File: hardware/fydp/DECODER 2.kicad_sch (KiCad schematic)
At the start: 29 parts, among them J2 Conn_01x02_Pin, J6 Conn_01x04_Pin, U55 74HC154D

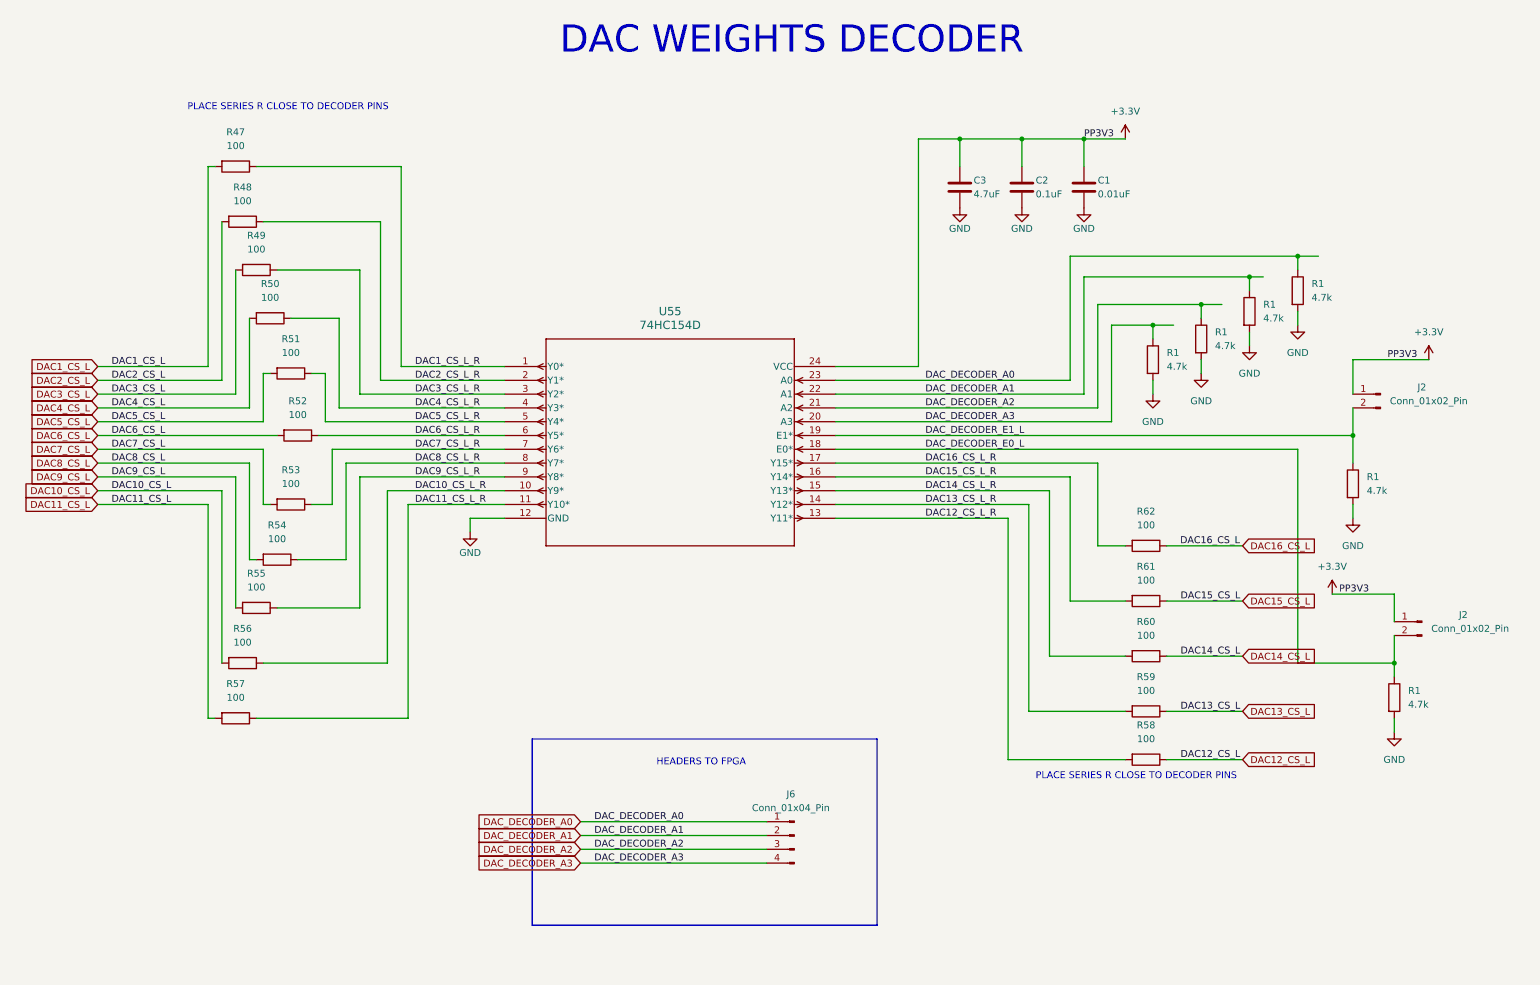
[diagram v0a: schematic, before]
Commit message: Remove 2 channels of multiplier and change ADC
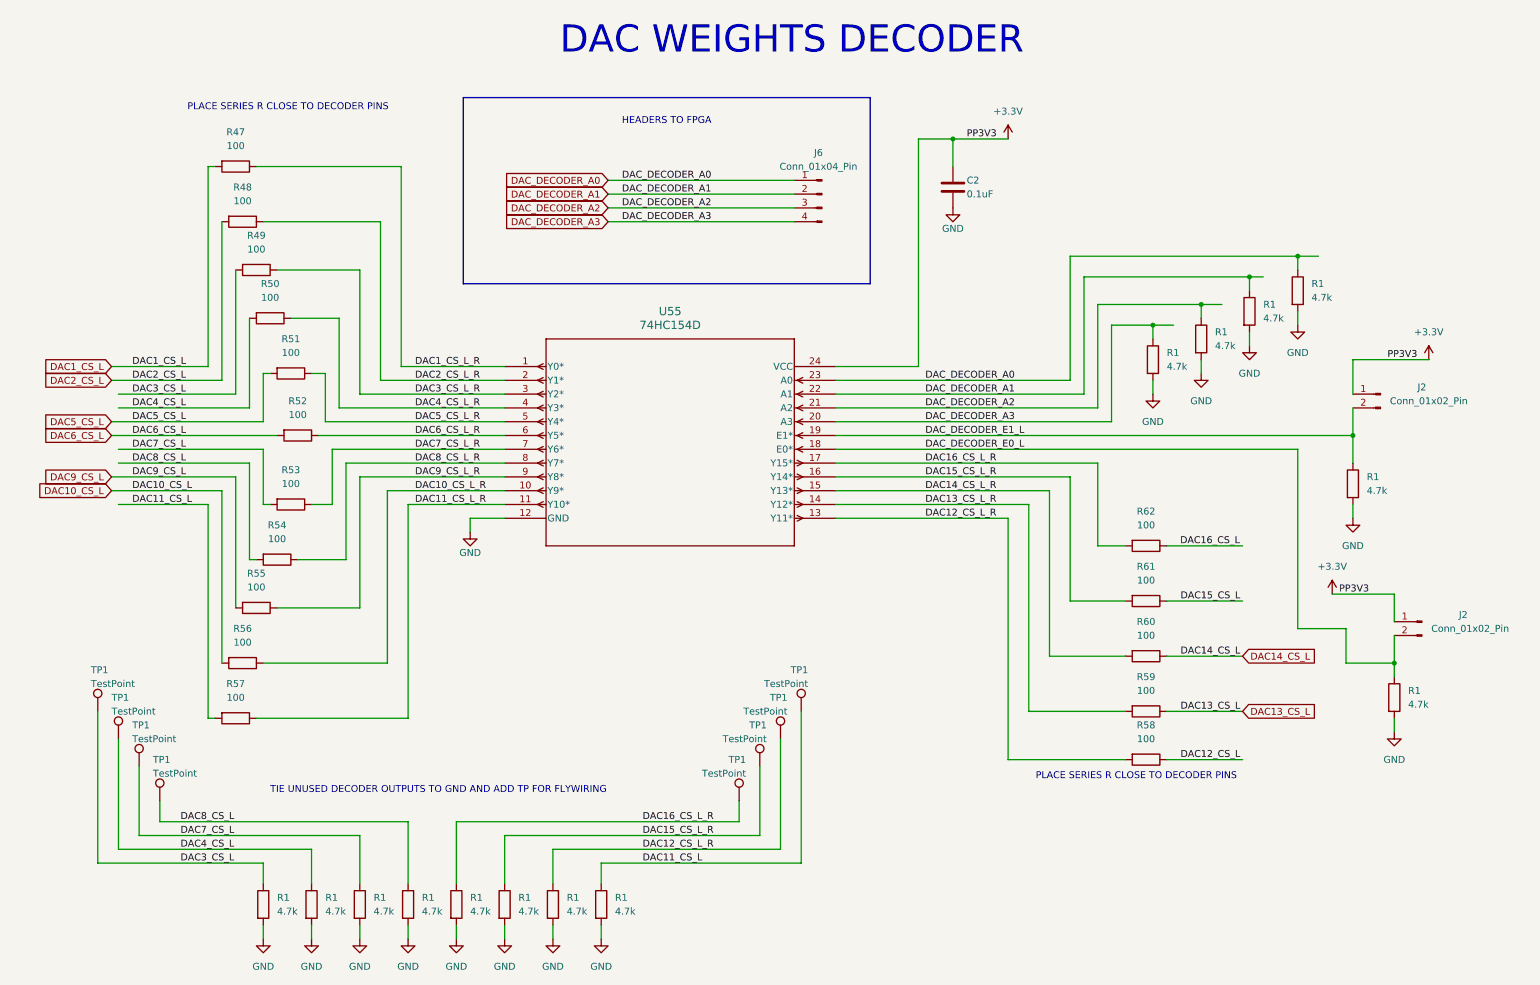
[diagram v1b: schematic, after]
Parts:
- removed C1: 0.01uF, Capacitor_SMD:C_0805_2012Metric, symbol Device:C
- removed C3: 4.7uF, Capacitor_SMD:C_0805_2012Metric, symbol Device:C
- added R1 (x8): 4.7k, Resistor_SMD:R_0805_2012Metric, symbol Device:R
- added TP1 (x8): TestPoint, TestPoint:TestPoint_Pad_1.0x1.0mm, symbol Connector:TestPoint
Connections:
- net DAC11_CS_L: now also R1.1, TP1.1
- net DAC12_CS_L_R: now also R1.1, TP1.1
- net DAC15_CS_L_R: now also R1.1, TP1.1
- net DAC16_CS_L_R: now also R1.1, TP1.1
- net DAC3_CS_L: now also R1.1, TP1.1
- net DAC4_CS_L: now also R1.1, TP1.1
- net DAC7_CS_L: now also R1.1, TP1.1
- net DAC8_CS_L: now also R1.1, TP1.1
- net GND: now also R1.2, R1.2, R1.2, R1.2, R1.2, R1.2, R1.2, R1.2
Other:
- note added: "TIE UNUSED DECODER OUTPUTS TO GND AND ADD TP FOR FLYWIRING"
- moved on the sheet: C2, J6

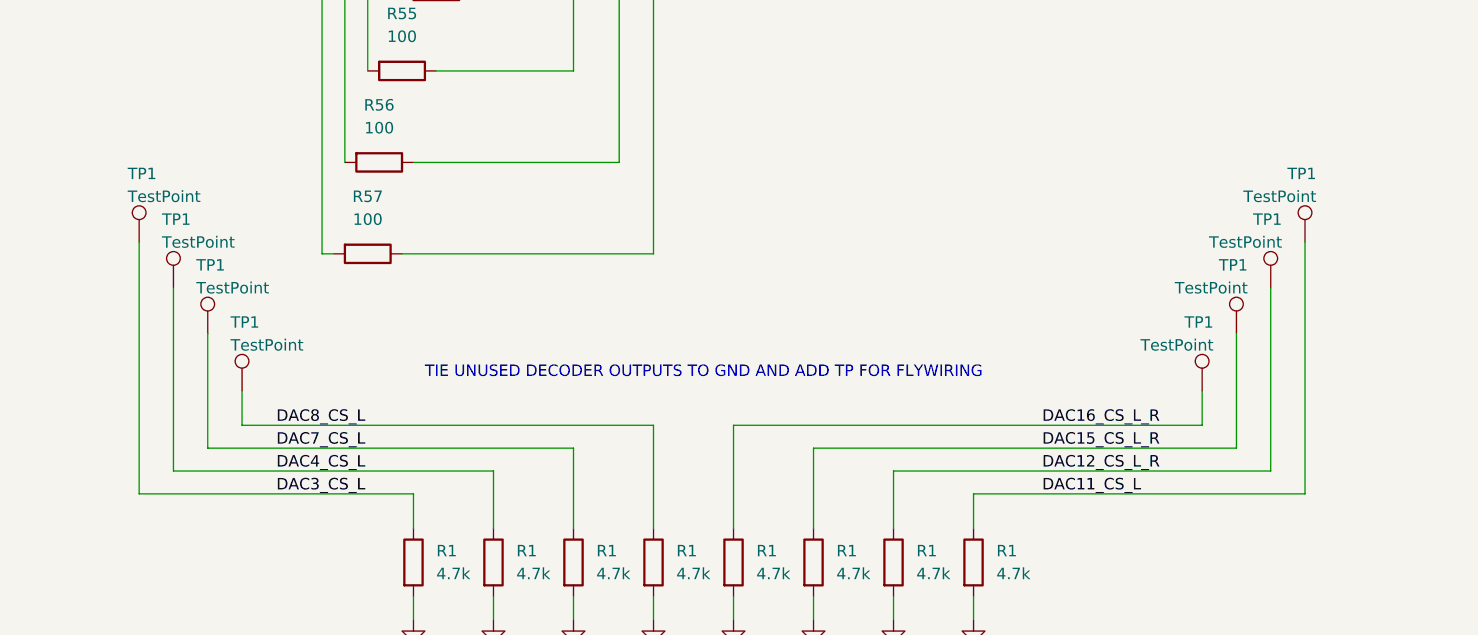
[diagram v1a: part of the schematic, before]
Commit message: Initial layout mostly complete, need to complete lots of routing
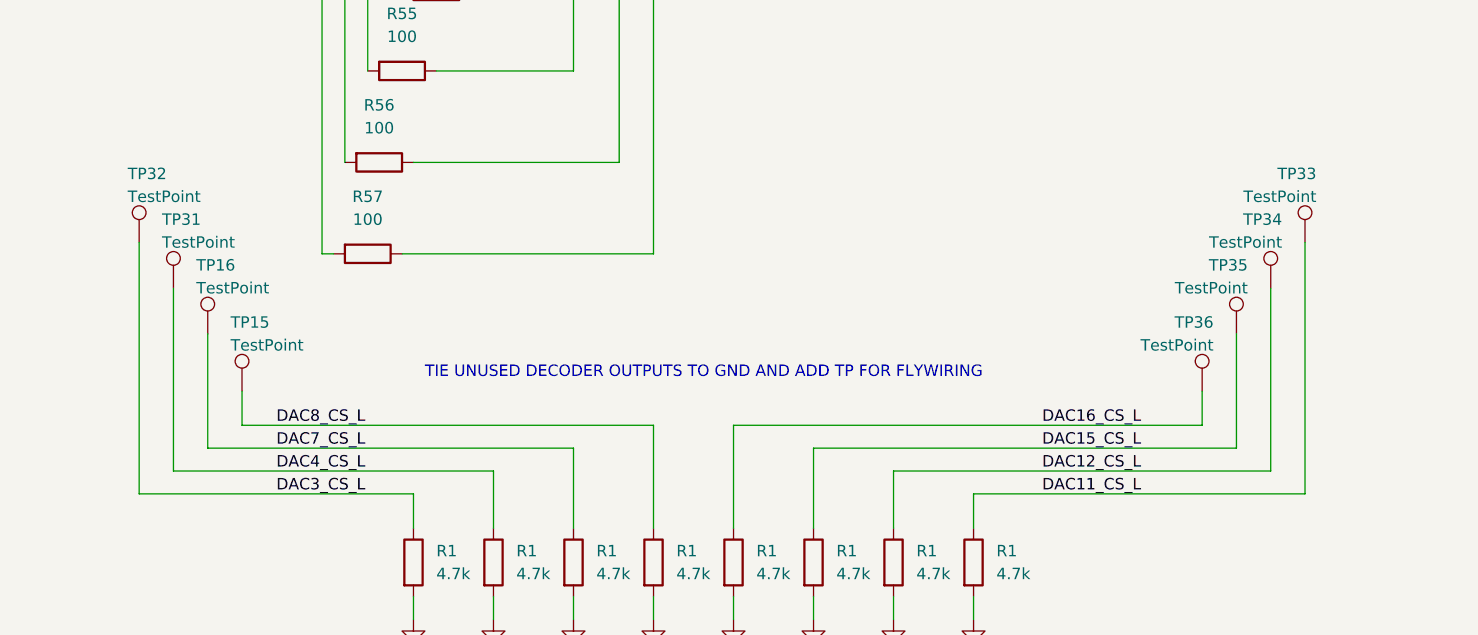
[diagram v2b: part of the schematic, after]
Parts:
- renumbered TP1 to TP15, TP1 to TP16, TP1 to TP31, TP1 to TP32, TP1 to TP33, TP1 to TP34, TP1 to TP35, TP1 to TP36
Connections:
- net DAC12_CS_L: now also R1.1, TP34.1
- net DAC12_CS_L_R: no longer R1.1, TP34.1
- net DAC15_CS_L: now also R1.1, TP35.1
- net DAC15_CS_L_R: no longer R1.1, TP35.1
- net DAC16_CS_L: now also R1.1, TP36.1
- net DAC16_CS_L_R: no longer R1.1, TP36.1
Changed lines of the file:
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@@
     (effects (font (size 1.27 1.27)) (justify left bottom))
   )
-  (label "DAC12_CS_L_R" (at 123.19 171.45 0) (fields_autoplaced)
+  (label "DAC12_CS_L" (at 123.19 171.45 0) (fields_autoplaced)
     (effects (font (size 1.27 1.27)) (justify left bottom))
   )
@@
     (effects (font (size 1.27 1.27)) (justify left bottom))
   )
-  (label "DAC15_CS_L_R" (at 123.19 168.91 0) (fields_autoplaced)
+  (label "DAC15_CS_L" (at 123.19 168.91 0) (fields_autoplaced)
     (effects (font (size 1.27 1.27)) (justify left bottom))
   )
@@
     (effects (font (size 1.27 1.27)) (justify left bottom))
   )
-  (label "DAC16_CS_L_R" (at 123.19 166.37 0) (fields_autoplaced)
+  (label "DAC16_CS_L" (at 123.19 166.37 0) (fields_autoplaced)
     (effects (font (size 1.27 1.27)) (justify left bottom))
   )
@@
   (symbol (lib_id "Connector:TestPoint") (at 30.48 156.21 0) (unit 1)
     (in_bom yes) (on_board yes) (dnp no)
-    (property "Reference" "TP1" (at 29.21 148.59 0)
+    (property "Reference" "TP16" (at 29.21 148.59 0)
       (effects (font (size 1.27 1.27)) (justify left))
     )
@@
   (symbol (lib_id "Connector:TestPoint") (at 148.59 151.13 0) (mirror y) (unit 1)
     (in_bom yes) (on_board yes) (dnp no)
-    (property "Reference" "TP1" (at 149.86 143.51 0)
+    (property "Reference" "TP34" (at 149.86 143.51 0)
       (effects (font (size 1.27 1.27)) (justify left))
     )
@@
   (symbol (lib_id "Connector:TestPoint") (at 22.86 146.05 0) (unit 1)
     (in_bom yes) (on_board yes) (dnp no)
-    (property "Reference" "TP1" (at 21.59 138.43 0)
+    (property "Reference" "TP32" (at 21.59 138.43 0)
       (effects (font (size 1.27 1.27)) (justify left))
     )
@@
   (symbol (lib_id "Connector:TestPoint") (at 26.67 151.13 0) (unit 1)
     (in_bom yes) (on_board yes) (dnp no)
-    (property "Reference" "TP1" (at 25.4 143.51 0)
+    (property "Reference" "TP31" (at 25.4 143.51 0)
       (effects (font (size 1.27 1.27)) (justify left))
     )
@@
   (symbol (lib_id "Connector:TestPoint") (at 34.29 162.56 0) (unit 1)
     (in_bom yes) (on_board yes) (dnp no)
-    (property "Reference" "TP1" (at 33.02 154.94 0)
+    (property "Reference" "TP15" (at 33.02 154.94 0)
       (effects (font (size 1.27 1.27)) (justify left))
     )
@@
   (symbol (lib_id "Connector:TestPoint") (at 140.97 162.56 0) (mirror y) (unit 1)
     (in_bom yes) (on_board yes) (dnp no)
-    (property "Reference" "TP1" (at 142.24 154.94 0)
+    (property "Reference" "TP36" (at 142.24 154.94 0)
       (effects (font (size 1.27 1.27)) (justify left))
     )
@@
   (symbol (lib_id "Connector:TestPoint") (at 152.4 146.05 0) (mirror y) (unit 1)
     (in_bom yes) (on_board yes) (dnp no)
-    (property "Reference" "TP1" (at 153.67 138.43 0)
+    (property "Reference" "TP33" (at 153.67 138.43 0)
       (effects (font (size 1.27 1.27)) (justify left))
     )
@@
   (symbol (lib_id "Connector:TestPoint") (at 144.78 156.21 0) (mirror y) (unit 1)
     (in_bom yes) (on_board yes) (dnp no)
-    (property "Reference" "TP1" (at 146.05 148.59 0)
-      (effects (font (size 1.27 1.27)) (justify left))
-    )
+    (property "Reference" "TP35" (at 146.05 148.59 0)
+      (effects (font (size 1.27 1.27)) (justify left))
+    )

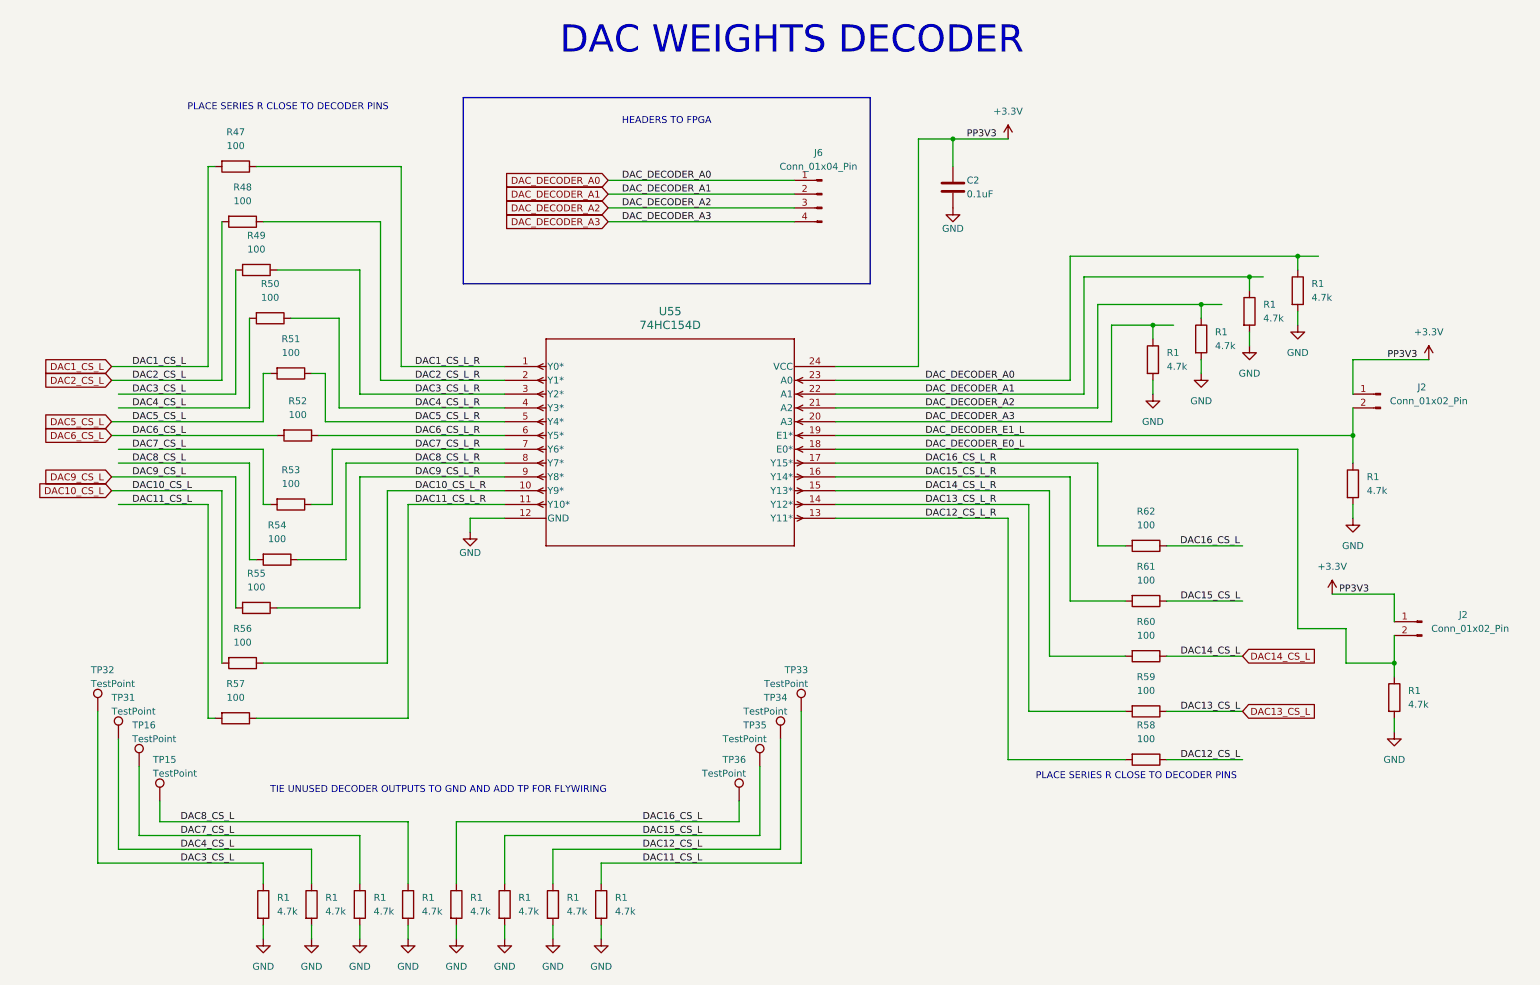
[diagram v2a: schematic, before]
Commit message: Completed placement and silk for left and centre sections of the PCB
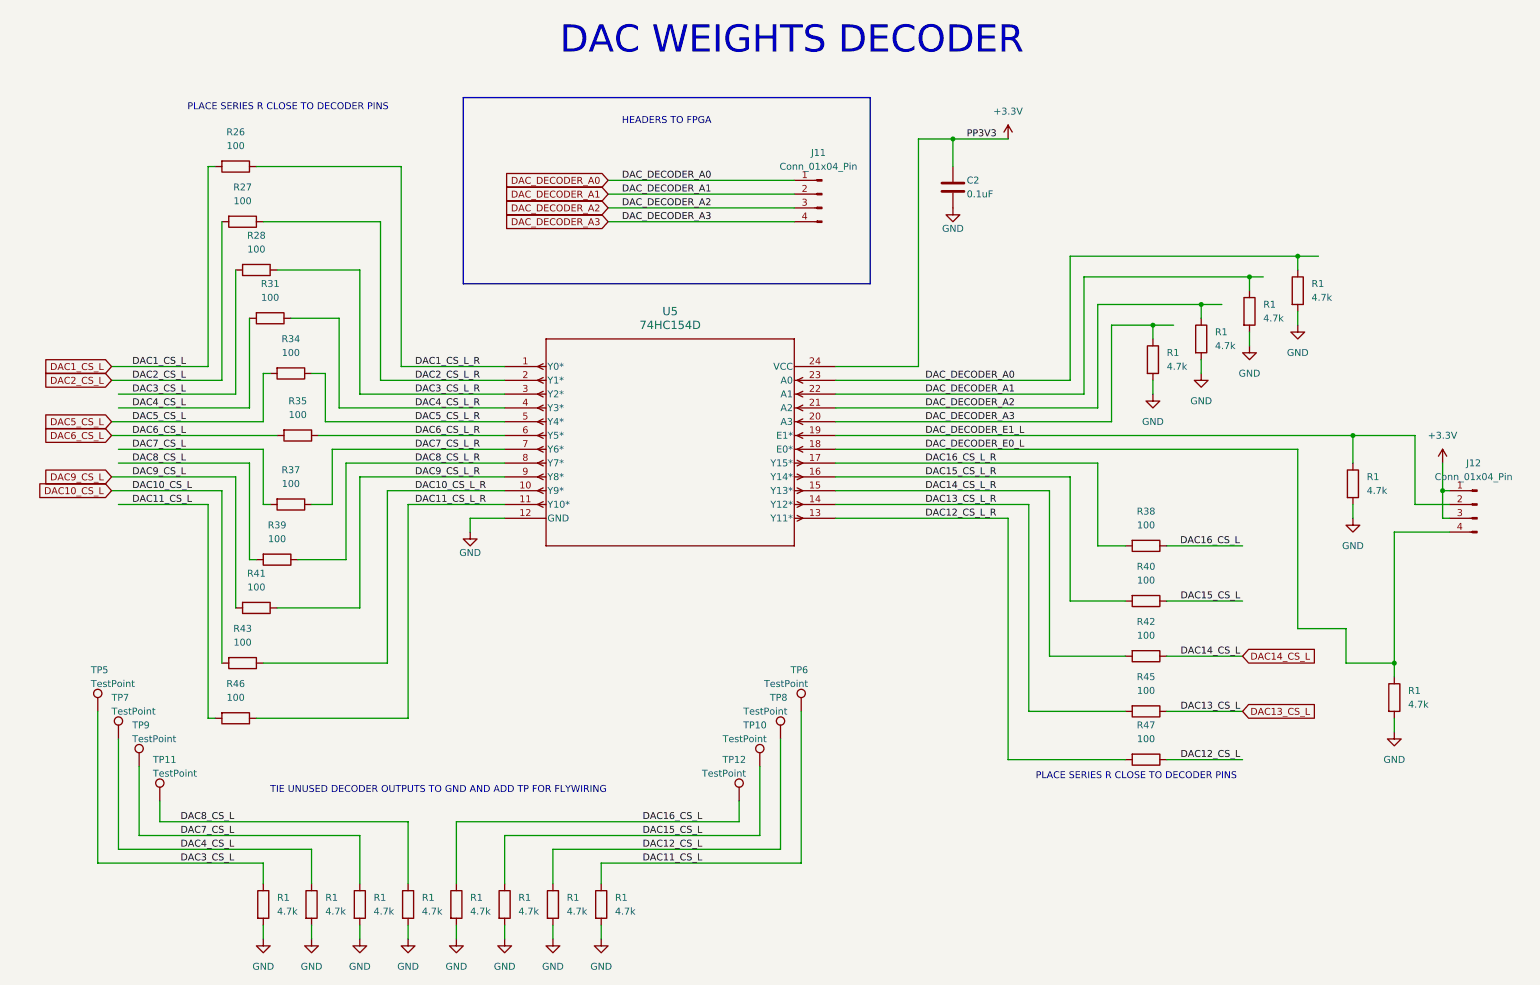
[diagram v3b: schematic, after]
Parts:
- removed J2 (x2): Conn_01x02_Pin, Connector_PinHeader_2.54mm:PinHeader_1x02_P2.54mm_Vertical, symbol Connector:Conn_01x02_Pin
- added J12: Conn_01x04_Pin, Connector_PinHeader_2.54mm:PinHeader_1x04_P2.54mm_Vertical, symbol Connector:Conn_01x04_Pin
- renumbered J6 to J11, R47 to R26, R48 to R27, R49 to R28, R50 to R31, R51 to R34, R52 to R35, R53 to R37, R62 to R38, R54 to R39, R61 to R40, R55 to R41, R60 to R42, R56 to R43, R59 to R45, R57 to R46, R58 to R47, TP35 to TP10, TP15 to TP11, TP36 to TP12, TP32 to TP5, TP33 to TP6, TP31 to TP7, TP34 to TP8, TP16 to TP9, U55 to U5
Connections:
- net +3.3V: now also J12.1 (Pin_1), J12.3 (Pin_3)
- net DAC_DECODER_E0_L: now also J12.4 (Pin_4)
- net DAC_DECODER_E1_L: now also J12.2 (Pin_2)

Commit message: Adding JLCPCB BOM notes
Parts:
- C2: Comment (none) -> 0.1 µF ±10% 50V Ceramic Capacitor X7R 0805 (2012 Metric); LCSC (none) -> C49678; MPN (none) -> CC0805KRX7R9BB104
- R1: Comment (none) -> 4.7 kOhms ±1% 0.125W, 1/8W Chip Resistor 0805 (2012 Metric)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; LCSC (none) -> C60816; MPN (none) -> RC0805FR-074K7L
- R26, R27, R28, R31, R34, R35, R37, R38, R39, R40, R41, R42, R43, R45, R46, R47: Comment (none) -> 100 Ohms ±1% 0.125W, 1/8W Chip Resistor 0805 (2012 Metric) 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; LCSC (none) -> C105577; MPN (none) -> RC0805FR-07100RL
